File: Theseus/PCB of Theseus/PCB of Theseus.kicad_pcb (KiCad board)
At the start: 4 copper layers, 45.2 x 70.6 mm, 87 parts, among them J1 G125-MH104M4-04AD000P, J2 4DB-P108-02, J3 CN4 STDC14 (Programmer), J4 Micro SD Holder 0472192001, J5 Conn_01x06_Socket, J6 Conn_01x06_Socket, J7 Conn_01x06_Socket, J8 Conn_01x06_Socket, Q1 DMG1012UW-7, Q2 DMG1012UW-7, U1 TPS565201DDC, U2 TCAN334, U3 STM32H750VBTx, U4 MX25L25645G, U5 MAX6675, Y1 ASE-4.000MHz-L-C-T

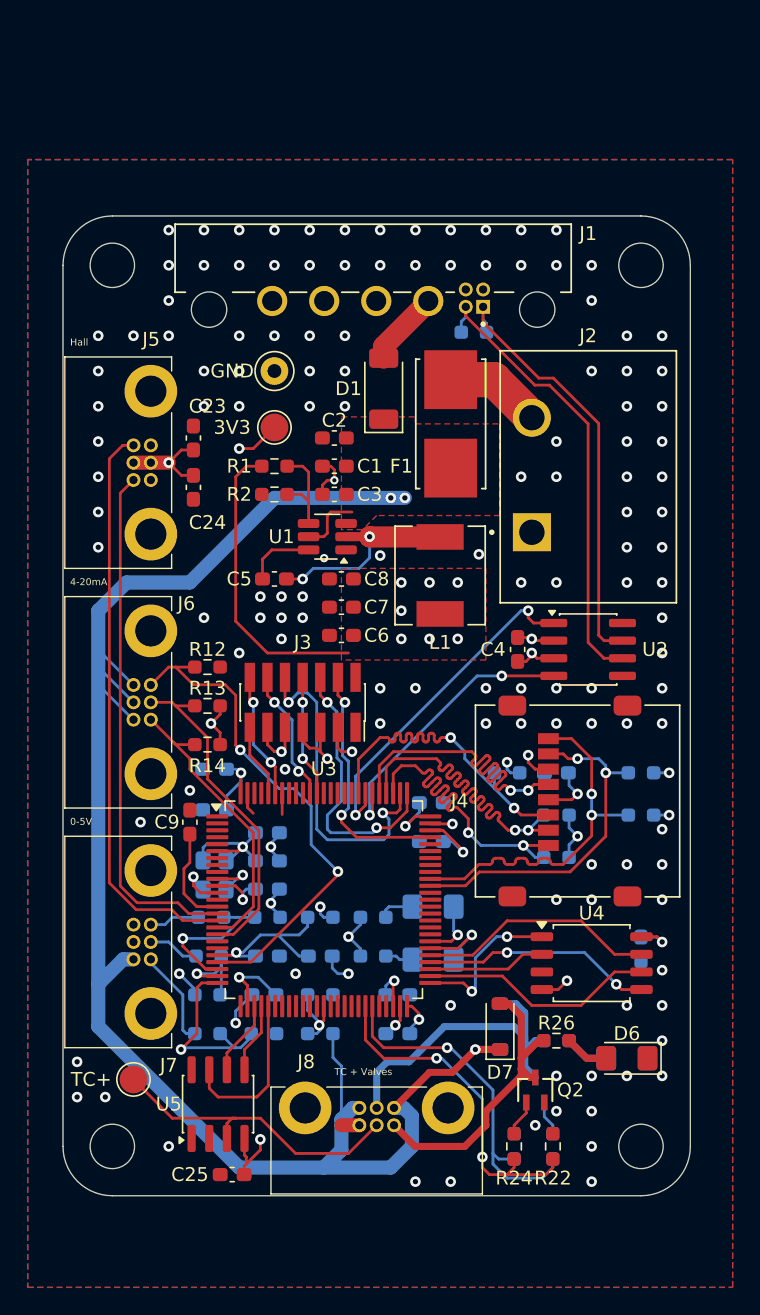
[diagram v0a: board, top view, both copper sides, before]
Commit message: Swapped out the h7 STM to a H503RBT. Should have retained all pin functionality and tried to maintain physical pin positions so routing should be similar
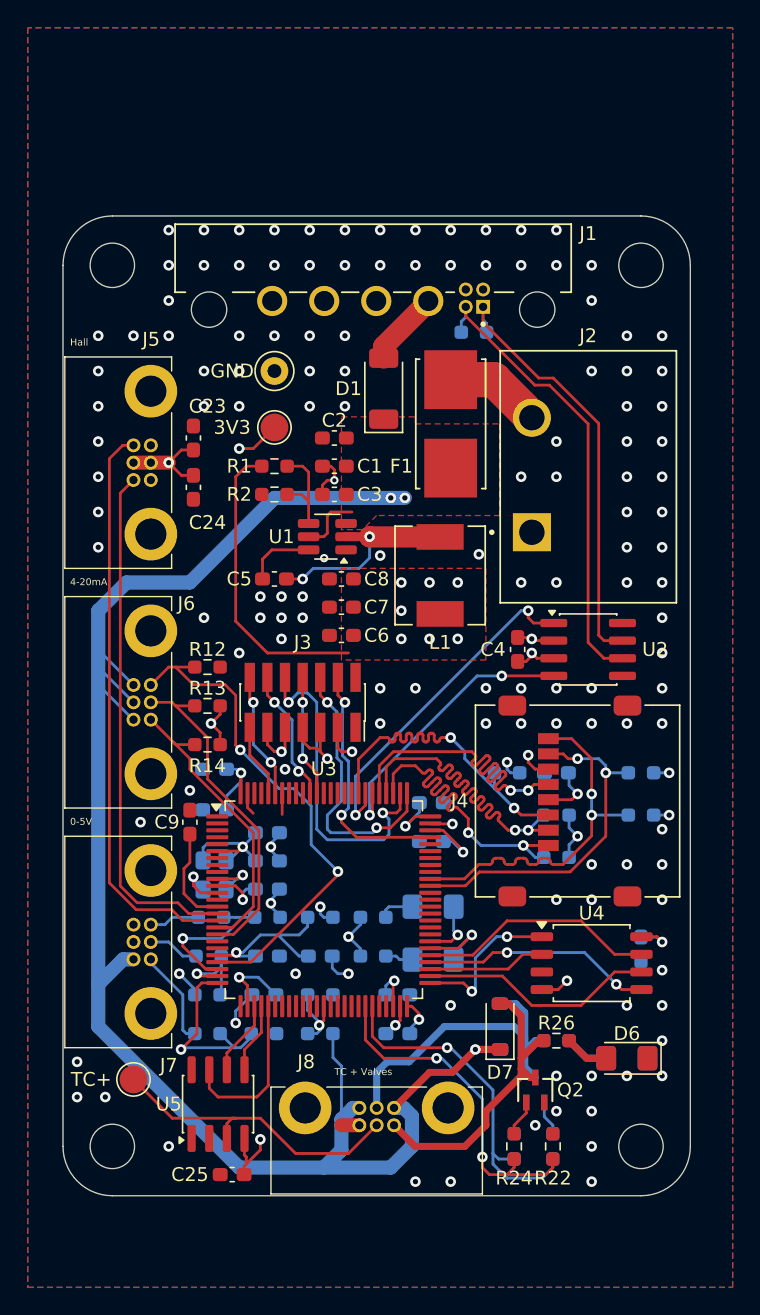
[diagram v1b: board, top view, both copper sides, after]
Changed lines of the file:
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@@
 		(min_thickness 0.25)
 		(filled_areas_thickness no)
-		(fill yes
+		(fill
 			(thermal_gap 0.5)
 			(thermal_bridge_width 0.5)
@@
 		(polygon
 			(pts
-				(xy 71.12 91.44) (xy 71.12 172.72) (xy 121.92 172.72) (xy 121.92 91.44)
+				(xy 71.12 81.94) (xy 71.12 172.72) (xy 121.92 172.72) (xy 121.92 81.94)
 			)
 		)
